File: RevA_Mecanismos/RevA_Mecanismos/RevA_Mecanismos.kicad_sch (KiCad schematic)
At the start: 31 parts, among them J1 Conn_01x02_Socket, J2 PROG, Q1 FDN335N, SW1 SW_Push, U1 STM32L431RCTx, Y1 16MHz

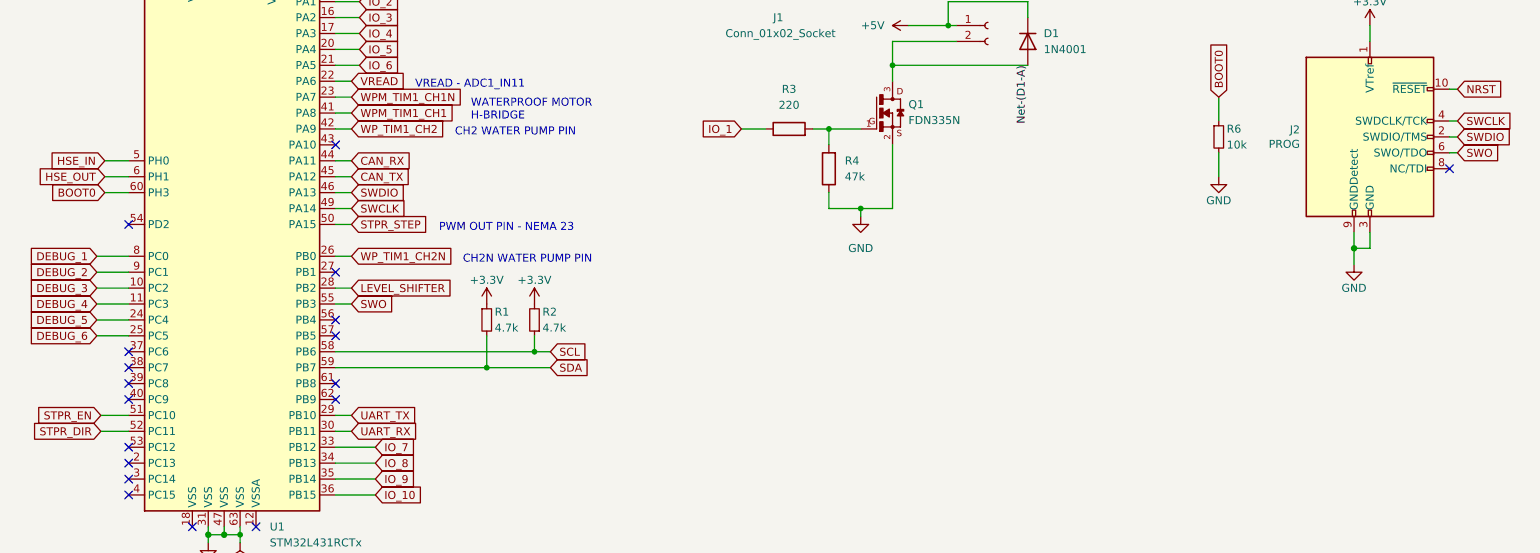
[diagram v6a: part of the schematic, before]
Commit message: Correction made to footprint for J3 pin header
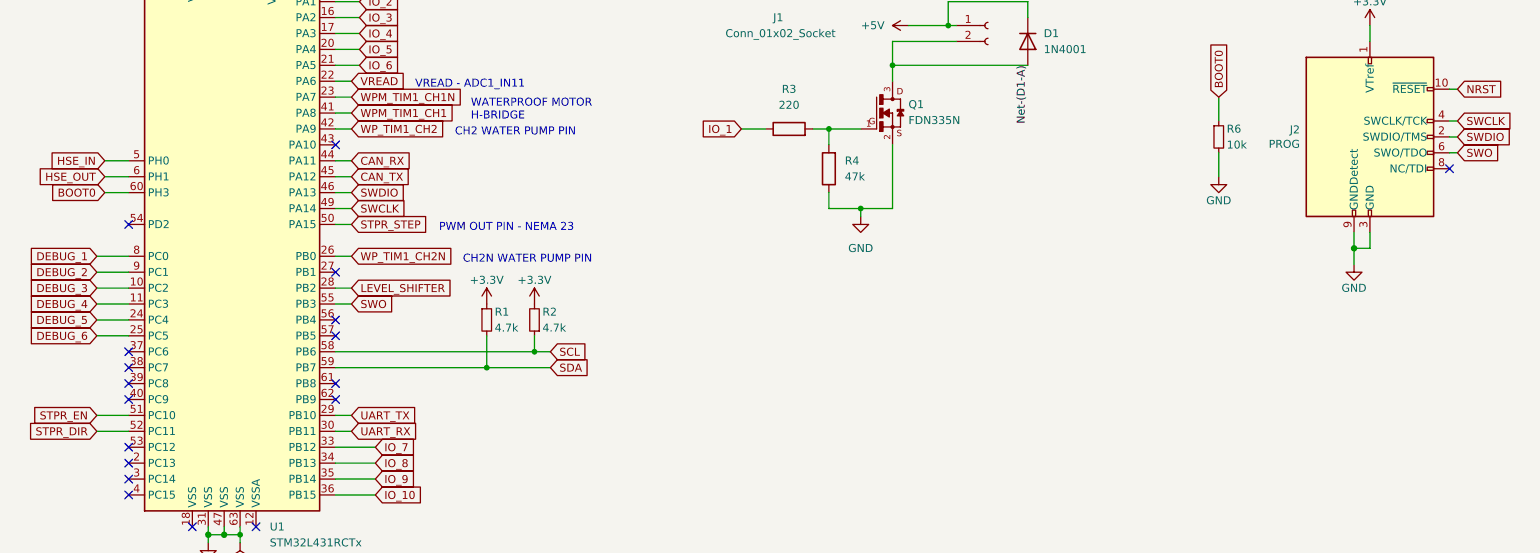
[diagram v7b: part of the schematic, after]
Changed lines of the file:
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@@
+    (stroke (width 0) (type default))
+  )
+  (wire (pts (xy 35.56 165.1) (xy 40.64 165.1))
     (stroke (width 0) (type default))
   )
@@
     (stroke (width 0) (type solid))
   )
-  (wire (pts (xy 36.195 165.1) (xy 40.64 165.1))
-    (stroke (width 0) (type default))
-  )
   (wire (pts (xy 97.79 154.94) (xy 107.95 154.94))
     (stroke (width 0) (type default))
@@
     (stroke (width 0) (type default))
   )
-  (wire (pts (xy 36.195 162.56) (xy 40.64 162.56))
-    (stroke (width 0) (type default))
-  )
   (wire (pts (xy 114.3 58.42) (xy 123.19 58.42))
     (stroke (width 0) (type default))
@@
   )
   (wire (pts (xy 97.79 154.94) (xy 97.79 149.86))
+    (stroke (width 0) (type default))
+  )
+  (wire (pts (xy 35.56 162.56) (xy 40.64 162.56))
     (stroke (width 0) (type default))
   )
@@
     )
   )
-  (global_label "STPR_DIR" (shape input) (at 36.195 165.1 180) (fields_autoplaced)
-    (effects (font (size 1.27 1.27)) (justify right))
-    (property "Intersheetrefs" "${INTERSHEET_REFS}" (at 24.3803 165.1 0)
+  (global_label "STPR_DIR" (shape input) (at 35.56 165.1 180) (fields_autoplaced)
+    (effects (font (size 1.27 1.27)) (justify right))
+    (property "Intersheetrefs" "${INTERSHEET_REFS}" (at 23.7453 165.1 0)
       (effects (font (size 1.27 1.27)) (justify right) hide)
     )
@@
     )
   )
-  (global_label "STPR_EN" (shape input) (at 36.195 162.56 180) (fields_autoplaced)
-    (effects (font (size 1.27 1.27)) (justify right))
-    (property "Intersheetrefs" "${INTERSHEET_REFS}" (at 25.0456 162.56 0)
-      (effects (font (size 1.27 1.27)) (justify right) hide)
-    )
+  (global_label "STPR_EN" (shape input) (at 35.56 162.56 180) (fields_autoplaced)
+    (effects (font (size 1.27 1.27)) (justify right))
+    (property "Intersheetrefs" "${INTERSHEET_REFS}" (at 24.4106 162.56 0)
+      (effects (font (size 1.27 1.27)) (justify right) hide)
+    )

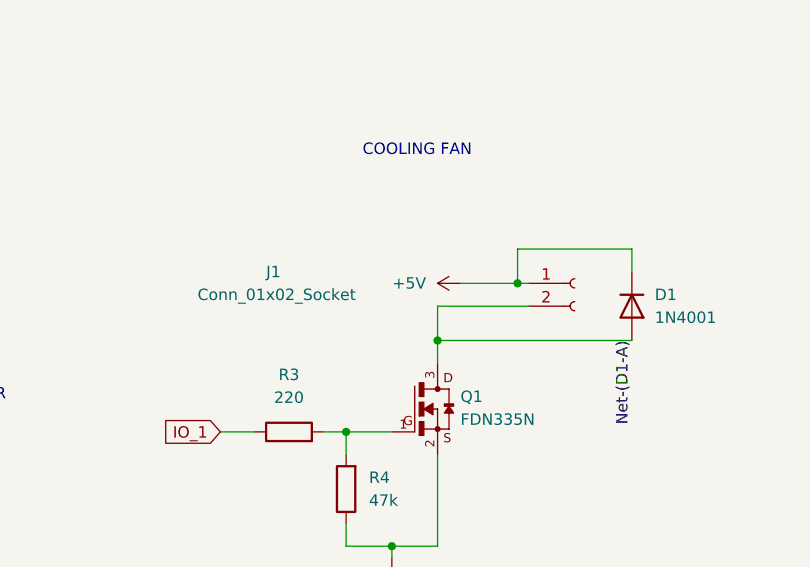
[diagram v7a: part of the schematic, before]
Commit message: Corrections to component footprints in schematic design made during the development of BOM
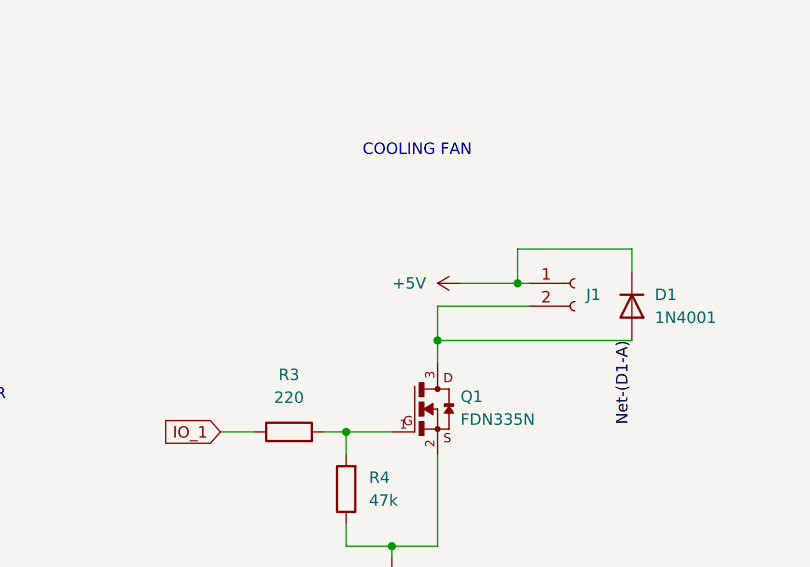
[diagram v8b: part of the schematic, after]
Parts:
- J1: value Conn_01x02_Socket -> Conn_01x02_Pin
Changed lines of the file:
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@@
   (symbol (lib_id "Connector:Conn_01x02_Socket") (at 177.8 100.33 0) (unit 1)
     (in_bom yes) (on_board yes) (dnp no)
-    (property "Reference" "J1" (at 143.51 99.06 0)
+    (property "Reference" "J1" (at 179.07 101.6 0)
       (effects (font (size 1.27 1.27)) (justify left))
     )
-    (property "Value" "Conn_01x02_Socket" (at 135.89 101.6 0)
-      (effects (font (size 1.27 1.27)) (justify left))
+    (property "Value" "Conn_01x02_Pin" (at 135.89 101.6 0)
+      (effects (font (size 1.27 1.27)) (justify left) hide)
     )
     (property "Footprint" "Connector_PinHeader_2.54mm:PinHeader_1x02_P2.54mm_Vertical" (at 177.8 100.33 0)
